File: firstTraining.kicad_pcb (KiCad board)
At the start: 2 copper layers, 11 parts, among them T1 Transformer_1P_SS, U1 TA48M05F, U2 TA48033S

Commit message: パターン配線
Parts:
- moved D2 1.27 mm to (127.0, 97.8)
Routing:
- net GND: track 0.00 -> 122.4 mm
- net Net-(C1-Pad1): track 0.00 -> 111.1 mm
- net Net-(D1-Pad1): track 0.00 -> 15.6 mm
- net Net-(D2-Pad1): track 0.00 -> 15.1 mm
- net Net-(C6-Pad1): track 0.00 -> 5.08 mm
- net Net-(C5-Pad1): track 0.00 -> 5.08 mm
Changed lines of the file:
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@@
     (thickness 1.6)
     (drawings 0)
-    (tracks 0)
+    (tracks 37)
     (zones 0)
     (modules 11)
@@
   )
   (module Diode_THT:D_A-405_P7.62mm_Horizontal (layer F.Cu)
-    (at 125.73 97.79)
+    (at 127 97.79)
     (descr "Diode, A-405 series, Axial, Horizontal, pin pitch=7.62mm, , length*diameter=5.2*2.7mm^2, , http://www.diodes.com/_files/packages/A-405.pdf")
     (tags "Diode A-405 series Axial Horizontal pin pitch 7.62mm  length 5.2mm diameter 2.7mm")
@@
     )
   )
+  (segment (start 134.62 97.79) (end 134.62 73.66) (width 0.25) (layer F.Cu) (net 1))
+  (segment (start 134.62 73.66) (end 149.86 73.66) (width 0.25) (layer F.Cu) (net 1))
+  (segment (start 149.86 73.66) (end 162.56 73.66) (width 0.25) (layer F.Cu) (net 1))
+  (segment (start 162.56 73.66) (end 176.53 73.66) (width 0.25) (layer F.Cu) (net 1))
+  (segment (start 176.53 73.66) (end 190.5 73.66) (width 0.25) (layer F.Cu) (net 1))
+  (segment (start 172.72 83.82) (end 176.53 87.63) (width 0.25) (layer F.Cu) (net 1))
+  (segment (start 172.72 78.72) (end 172.72 83.82) (width 0.25) (layer F.Cu) (net 1))
+  (segment (start 176.53 74.91) (end 172.72 78.72) (width 0.25) (layer F.Cu) (net 1))
+  (segment (start 176.53 73.66) (end 176.53 74.91) (width 0.25) (layer F.Cu) (net 1))
+  (segment (start 190.5 87.63) (end 176.53 87.63) (width 0.25) (layer F.Cu) (net 1))
+  (segment (start 180.34 88.9) (end 180.26 88.9) (width 0.25) (layer F.Cu) (net 2))
+  (segment (start 165.06 78.66) (end 162.56 76.16) (width 0.25) (layer B.Cu) (net 2))
+  (segment (start 176.53 78.66) (end 165.06 78.66) (width 0.25) (layer B.Cu) (net 2))
+  (segment (start 142.16 86.36) (end 149.86 78.66) (width 0.25) (layer B.Cu) (net 2))
+  (segment (start 114.87 86.36) (end 142.16 86.36) (width 0.25) (layer B.Cu) (net 2))
+  (segment (start 160.06 78.66) (end 162.56 76.16) (width 0.25) (layer B.Cu) (net 2))
+  (segment (start 149.86 78.66) (end 160.06 78.66) (width 0.25) (layer B.Cu) (net 2))
+  (segment (start 176.53 78.66) (end 180.34 82.47) (width 0.25) (layer B.Cu) (net 2))
+  (segment (start 180.34 82.47) (end 180.34 88.9) (width 0.25) (layer B.Cu) (net 2))
+  (segment (start 180.26 88.9) (end 176.53 92.63) (width 0.25) (layer B.Cu) (net 2))
+  (segment (start 180.34 88.9) (end 180.26 88.9) (width 0.25) (layer B.Cu) (net 2))
+  (segment (start 190.42 78.66) (end 190.5 78.74) (width 0.25) (layer B.Cu) (net 2))
+  (segment (start 176.53 78.66) (end 190.42 78.66) (width 0.25) (layer B.Cu) (net 2))
+  (segment (start 190.42 92.63) (end 190.5 92.71) (width 0.25) (layer B.Cu) (net 2))
+  (segment (start 176.53 92.63) (end 190.42 92.63) (width 0.25) (layer B.Cu) (net 2))
+  (segment (start 195.54 92.71) (end 195.58 92.67) (width 0.25) (layer B.Cu) (net 2))
+  (segment (start 190.5 92.71) (end 195.54 92.71) (width 0.25) (layer B.Cu) (net 2))
+  (segment (start 190.54 78.7) (end 190.5 78.74) (width 0.25) (layer B.Cu) (net 2))
+  (segment (start 195.58 78.7) (end 190.54 78.7) (width 0.25) (layer B.Cu) (net 2))
+  (segment (start 195.58 76.2) (end 190.5 76.2) (width 0.25) (layer F.Cu) (net 3))
+  (segment (start 190.5 90.17) (end 195.58 90.17) (width 0.25) (layer F.Cu) (net 4))
+  (segment (start 127 74.81) (end 127 73.66) (width 0.25) (layer F.Cu) (net 5))
+  (segment (start 121.45 80.36) (end 127 74.81) (width 0.25) (layer F.Cu) (net 5))
+  (segment (start 114.87 80.36) (end 121.45 80.36) (width 0.25) (layer F.Cu) (net 5))
+  (segment (start 122.72 92.36) (end 127 96.64) (width 0.25) (layer F.Cu) (net 6))
+  (segment (start 127 96.64) (end 127 97.79) (width 0.25) (layer F.Cu) (net 6))
+  (segment (start 114.87 92.36) (end 122.72 92.36) (width 0.25) (layer F.Cu) (net 6))
 )

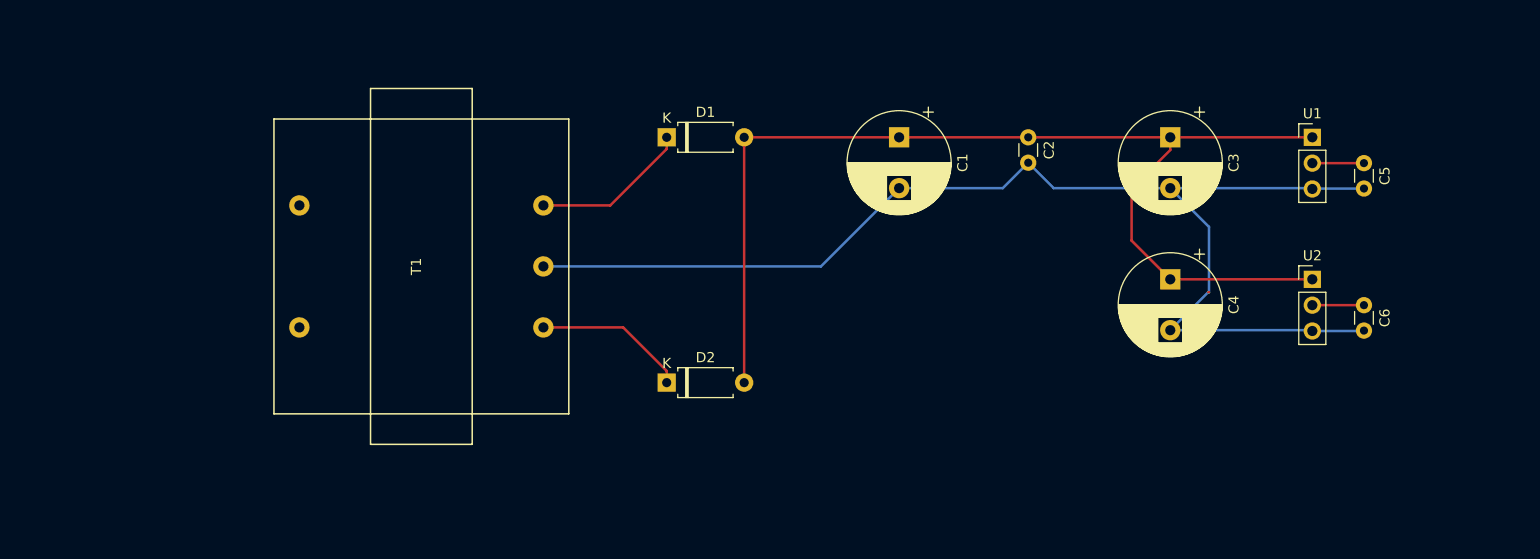
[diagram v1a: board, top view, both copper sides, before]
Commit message: GNDベタ
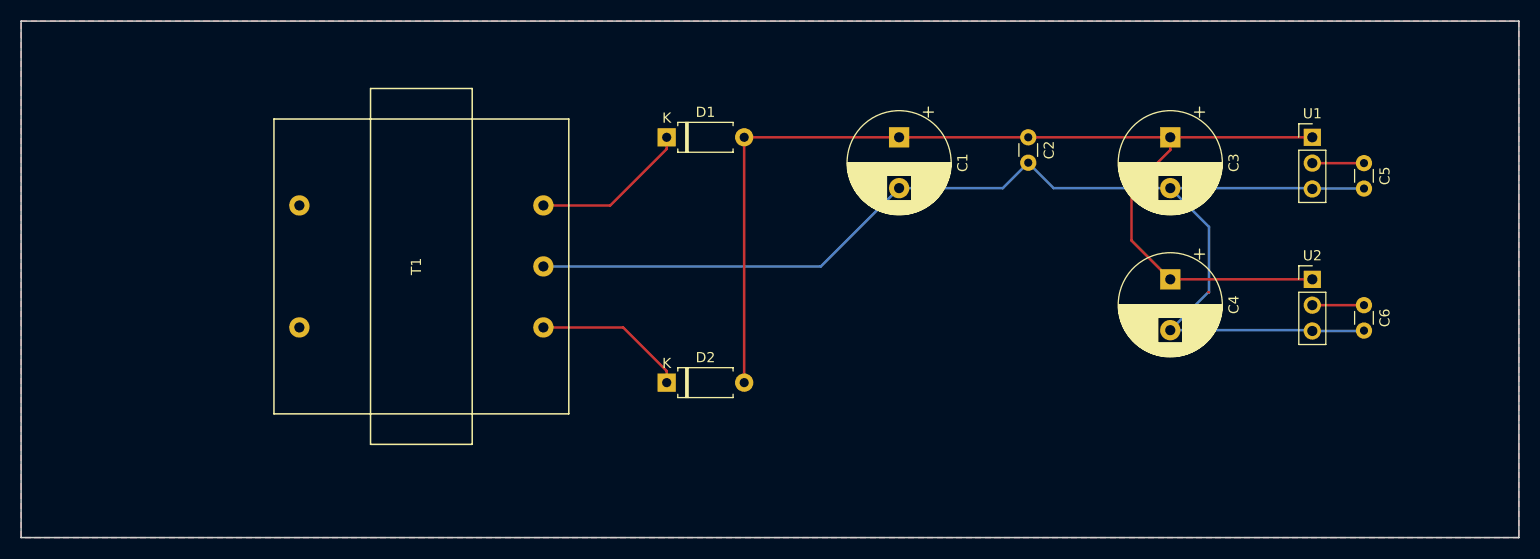
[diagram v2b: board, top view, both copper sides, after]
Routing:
- added copper zone on B.Cu, net GND
- added copper zone on F.Cu, net GND
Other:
- board outline added: 147.3 x 50.8 mm
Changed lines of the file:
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@@
   (general
     (thickness 1.6)
-    (drawings 0)
+    (drawings 4)
     (tracks 37)
     (zones 0)
@@
     )
   )
+  (gr_line (start 63.5 113.03) (end 63.5 62.23) (layer Edge.Cuts) (width 0.15))
+  (gr_line (start 63.5 62.23) (end 210.82 62.23) (layer Edge.Cuts) (width 0.15))
+  (gr_line (start 210.82 113.03) (end 210.82 62.23) (layer Edge.Cuts) (width 0.15))
+  (gr_line (start 63.5 113.03) (end 210.82 113.03) (layer Edge.Cuts) (width 0.15))
   (segment (start 134.62 97.79) (end 134.62 73.66) (width 0.25) (layer F.Cu) (net 1))
   (segment (start 134.62 73.66) (end 149.86 73.66) (width 0.25) (layer F.Cu) (net 1))
@@
   (segment (start 127 96.64) (end 127 97.79) (width 0.25) (layer F.Cu) (net 6))
   (segment (start 114.87 92.36) (end 122.72 92.36) (width 0.25) (layer F.Cu) (net 6))
+  (zone (net 2) (net_name GND) (layer F.Cu) (hatch edge 0.508)
+    (connect_pads (clearance 0.508))
+    (min_thickness 0.254)
+    (fill yes (arc_segments 16) (thermal_gap 0.508) (thermal_bridge_width 0.508))
+    (polygon
+      (pts
+        (xy 63.5 62.23) (xy 210.82 62.23) (xy 210.82 113.03) (xy 63.5 113.03)
+      )
+    )
+  )
+  (zone (net 2) (net_name GND) (layer B.Cu) (hatch edge 0.508)
+    (connect_pads (clearance 0.508))
+    (min_thickness 0.254)
+    (fill yes (arc_segments 16) (thermal_gap 0.508) (thermal_bridge_width 0.508))
+    (polygon
+      (pts
+        (xy 63.5 62.23) (xy 210.82 62.23) (xy 210.82 113.03) (xy 63.5 113.03)
+      )
+    )
+  )
 )

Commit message: パターン状にビアを追加
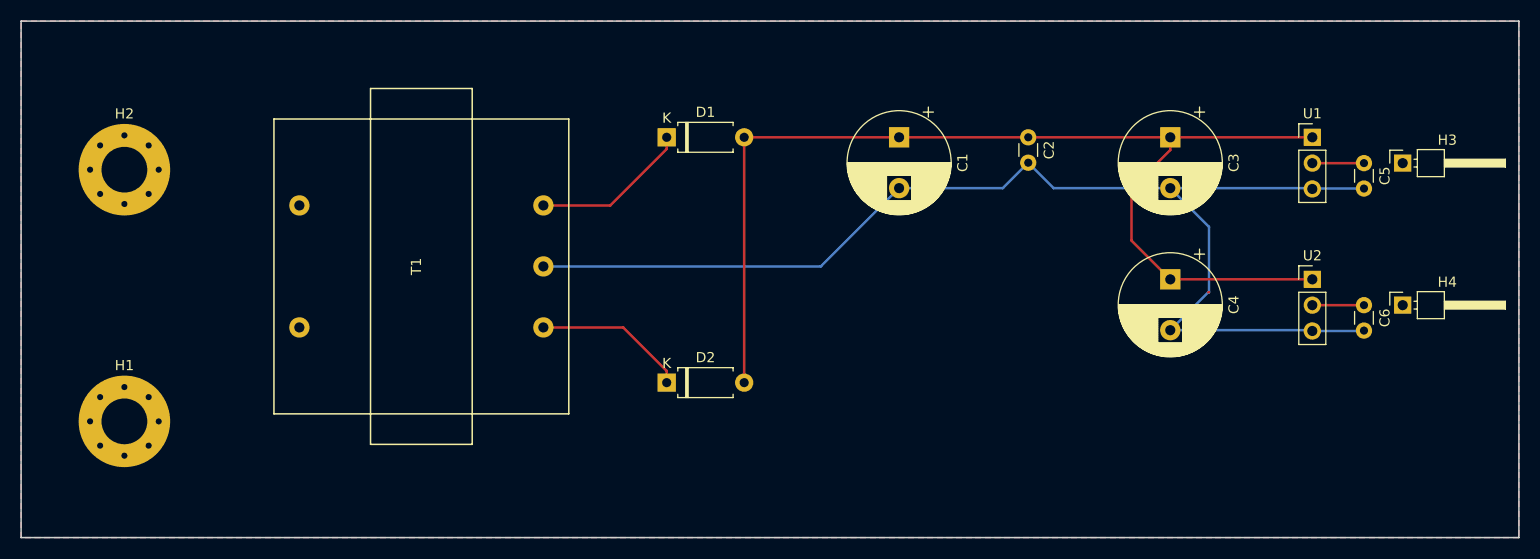
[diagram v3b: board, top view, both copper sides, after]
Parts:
- added H1: MountingHole_Pad, MountingHole:MountingHole_4.5mm_Pad_Via, F.Cu at (73.7, 101.6)
- added H2: MountingHole_Pad, MountingHole:MountingHole_4.5mm_Pad_Via, F.Cu at (73.7, 76.8)
- added H3: MountingHole_Pad, Connector_PinHeader_2.54mm:PinHeader_1x01_P2.54mm_Horizontal, F.Cu at (199.4, 76.2)
- added H4: MountingHole_Pad, Connector_PinHeader_2.54mm:PinHeader_1x01_P2.54mm_Horizontal, F.Cu at (199.4, 90.2)
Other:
- net class Default: clearance 0.2 -> 0.254; trace_width 0.25 -> 0.254
- rule trace_clearance: 0.2 -> 0.254
- rule via_min_drill: 0.3 -> 0.4
- rule via_min_size: 0.4 -> 0.8

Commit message: GNDビアを追加
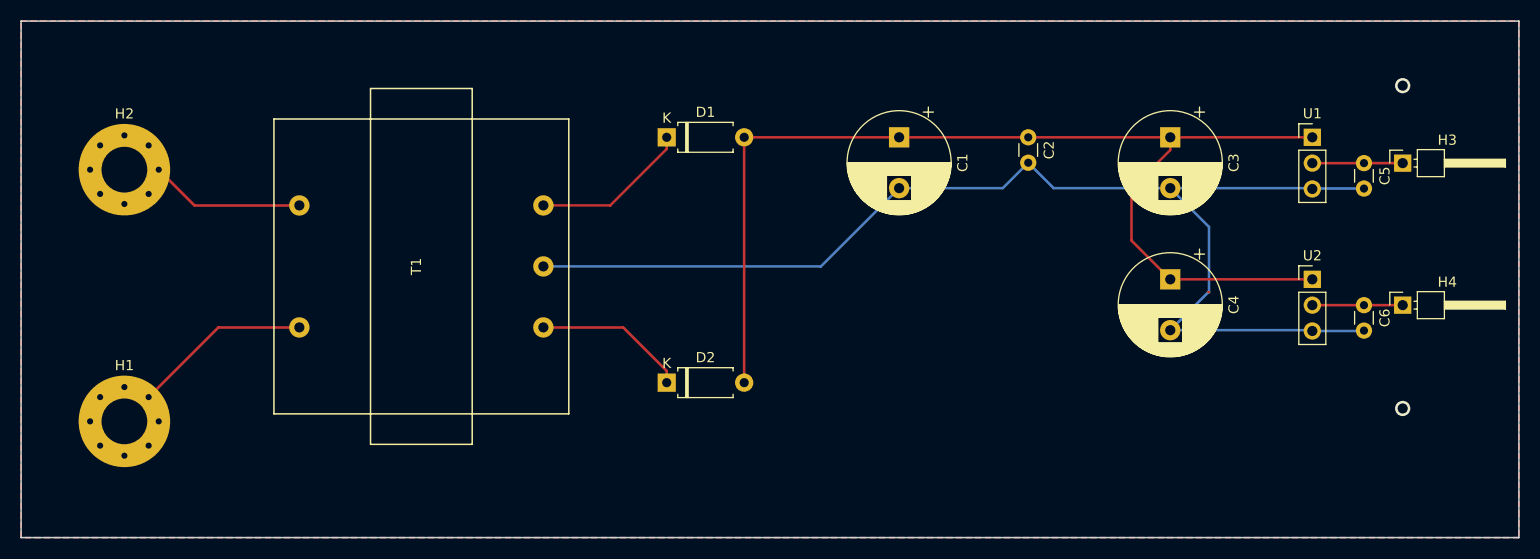
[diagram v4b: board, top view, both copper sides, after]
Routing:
- net AC: track 0.00 -> 17.7 mm
- net Net-(H2-Pad1): track 0.00 -> 15.3 mm
- net Net-(C6-Pad1): track 5.08 -> 8.89 mm
- net Net-(C5-Pad1): track 5.08 -> 8.89 mm
- net GND: vias 0 -> 2
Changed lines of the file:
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@@
     (thickness 1.6)
     (drawings 4)
-    (tracks 37)
+    (tracks 46)
     (zones 0)
     (modules 15)
@@
   (segment (start 190.54 78.7) (end 190.5 78.74) (width 0.25) (layer B.Cu) (net 2))
   (segment (start 195.58 78.7) (end 190.54 78.7) (width 0.25) (layer B.Cu) (net 2))
+  (via (at 199.39 100.33) (size 1.5) (drill 1) (layers F.Cu B.Cu) (net 2))
+  (via (at 199.39 68.58) (size 1.5) (drill 1) (layers F.Cu B.Cu) (net 2))
   (segment (start 195.58 76.2) (end 190.5 76.2) (width 0.25) (layer F.Cu) (net 3))
+  (segment (start 199.39 76.2) (end 195.58 76.2) (width 0.254) (layer F.Cu) (net 3))
   (segment (start 190.5 90.17) (end 195.58 90.17) (width 0.25) (layer F.Cu) (net 4))
+  (segment (start 199.39 90.17) (end 195.58 90.17) (width 0.254) (layer F.Cu) (net 4))
   (segment (start 127 74.81) (end 127 73.66) (width 0.25) (layer F.Cu) (net 5))
   (segment (start 121.45 80.36) (end 127 74.81) (width 0.25) (layer F.Cu) (net 5))
@@
   (segment (start 127 96.64) (end 127 97.79) (width 0.25) (layer F.Cu) (net 6))
   (segment (start 114.87 92.36) (end 122.72 92.36) (width 0.25) (layer F.Cu) (net 6))
+  (segment (start 82.9 92.36) (end 76.046485 99.213515) (width 0.254) (layer F.Cu) (net 7))
+  (segment (start 90.87 92.36) (end 82.9 92.36) (width 0.254) (layer F.Cu) (net 7))
+  (segment (start 77.484999 77.295) (end 77.035 76.845001) (width 0.254) (layer F.Cu) (net 8))
+  (segment (start 80.549999 80.36) (end 77.484999 77.295) (width 0.254) (layer F.Cu) (net 8))
+  (segment (start 90.87 80.36) (end 80.549999 80.36) (width 0.254) (layer F.Cu) (net 8))
   (zone (net 2) (net_name GND) (layer F.Cu) (hatch edge 0.508)
     (connect_pads (clearance 0.508))
+    (min_thickness 0.254)
+    (fill yes (arc_segments 16) (thermal_gap 0.508) (thermal_bridge_width 0.508))
+    (polygon
+      (pts
+        (xy 63.5 62.23) (xy 210.82 62.23) (xy 210.82 113.03) (xy 63.5 113.03)
+      )
+    )
+  )
+  (zone (net 2) (net_name GND) (layer B.Cu) (hatch edge 0.508)
+    (connect_pads (clearance 0.508))
+    (min_thickness 0.254)
+    (fill yes (arc_segments 16) (thermal_gap 0.508) (thermal_bridge_width 0.508))
+    (polygon
+      (pts
+        (xy 63.5 62.23) (xy 210.82 62.23) (xy 210.82 113.03) (xy 63.5 113.03)
+      )
+    )
+  )
+  (zone (net 2) (net_name GND) (layer F.Cu) (hatch edge 0.508)
+    (connect_pads (clearance 0.508))

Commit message: pcbのgndベタを修正
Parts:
- added H5: MountingHole_Pad, Connector_PinHeader_2.54mm:PinHeader_1x01_P2.54mm_Horizontal, F.Cu at (199.4, 67.3)
- added H6: MountingHole_Pad, Connector_PinHeader_2.54mm:PinHeader_1x01_P2.54mm_Horizontal, F.Cu at (199.4, 100.3)
- D1, D2: value DIODE -> D
- moved D1 7.62 mm to (134.6, 73.7), turned to 180 degrees
- moved D2 7.62 mm to (134.6, 97.8), turned to 180 degrees
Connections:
- D1 pad 1: Net-(D1-Pad1) -> Net-(C1-Pad1)
- D1 pad 2: Net-(C1-Pad1) -> Net-(D1-Pad2)
- D2 pad 1: Net-(D2-Pad1) -> Net-(C1-Pad1)
- D2 pad 2: Net-(C1-Pad1) -> Net-(D2-Pad2)
- T1 pad 3: Net-(D1-Pad1) -> Net-(D1-Pad2)
- T1 pad 5: Net-(D2-Pad1) -> Net-(D2-Pad2)
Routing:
- net Net-(D1-Pad2): track 0.00 -> 16.1 mm
- net Net-(D1-Pad1): track 15.6 -> 0.00 mm
- net Net-(D2-Pad2): track 0.00 -> 15.5 mm
- net Net-(D2-Pad1): track 15.1 -> 0.00 mm
- net GND: vias 2 -> 0
